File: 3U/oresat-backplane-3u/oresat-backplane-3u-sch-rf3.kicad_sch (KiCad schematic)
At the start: 30 parts

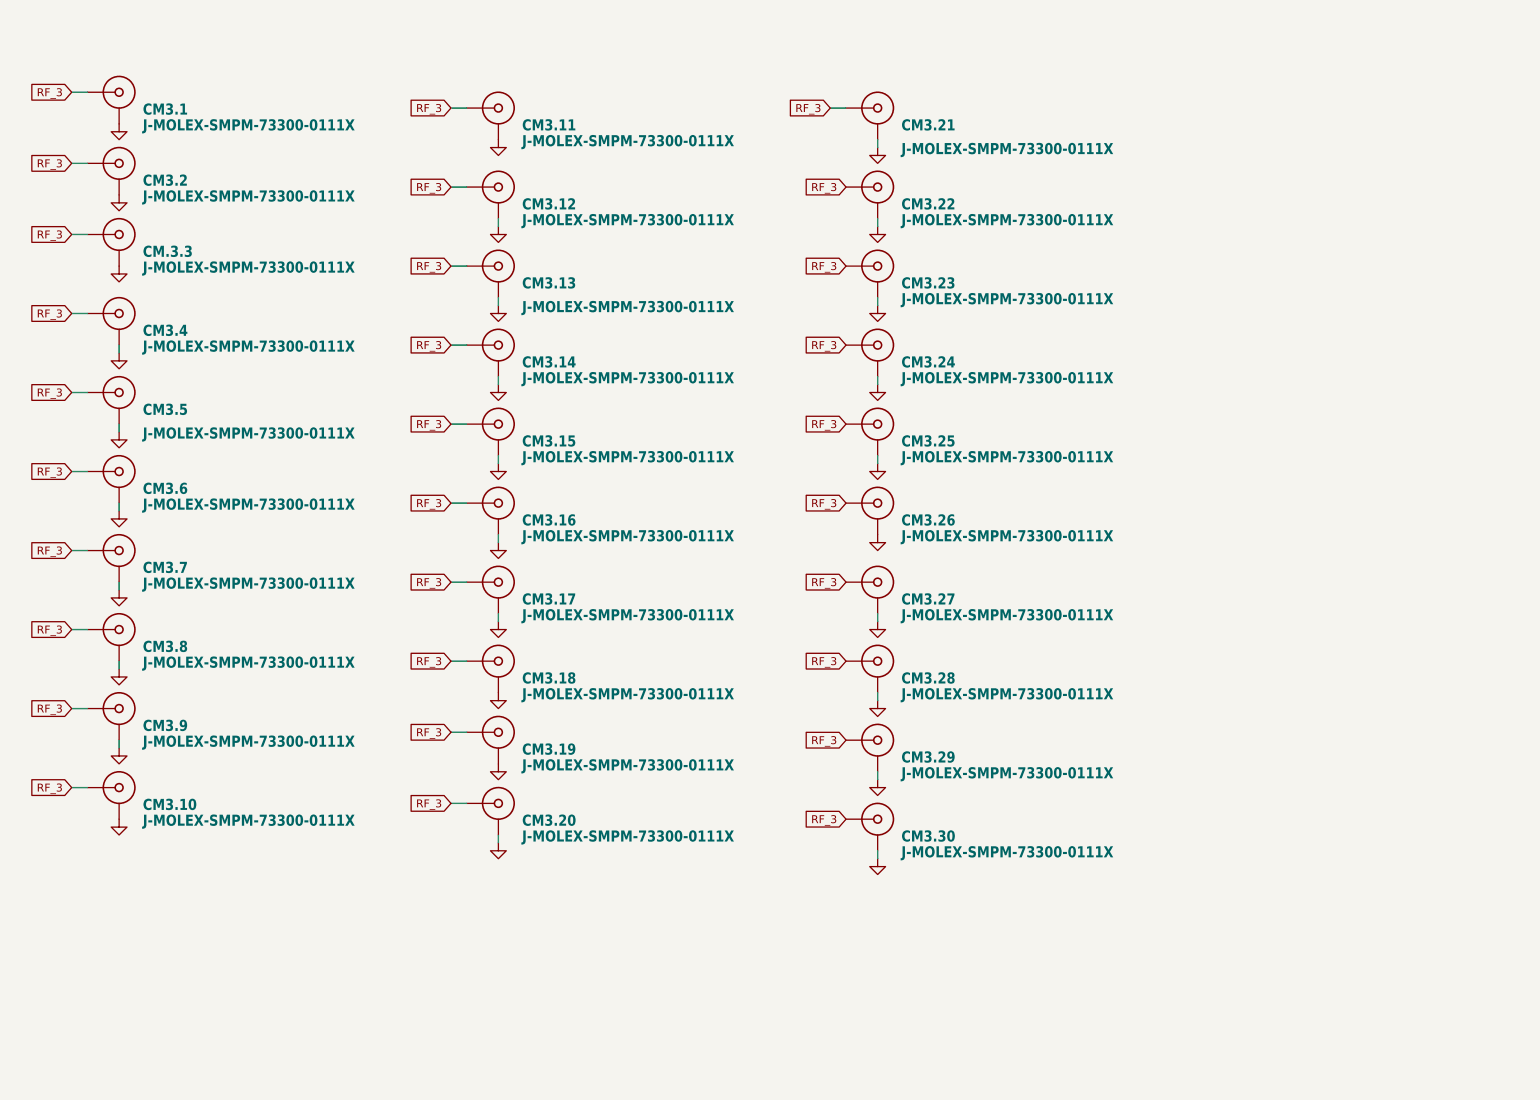
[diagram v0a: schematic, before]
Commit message: Moved can lines to back & fixed RF schematic organization
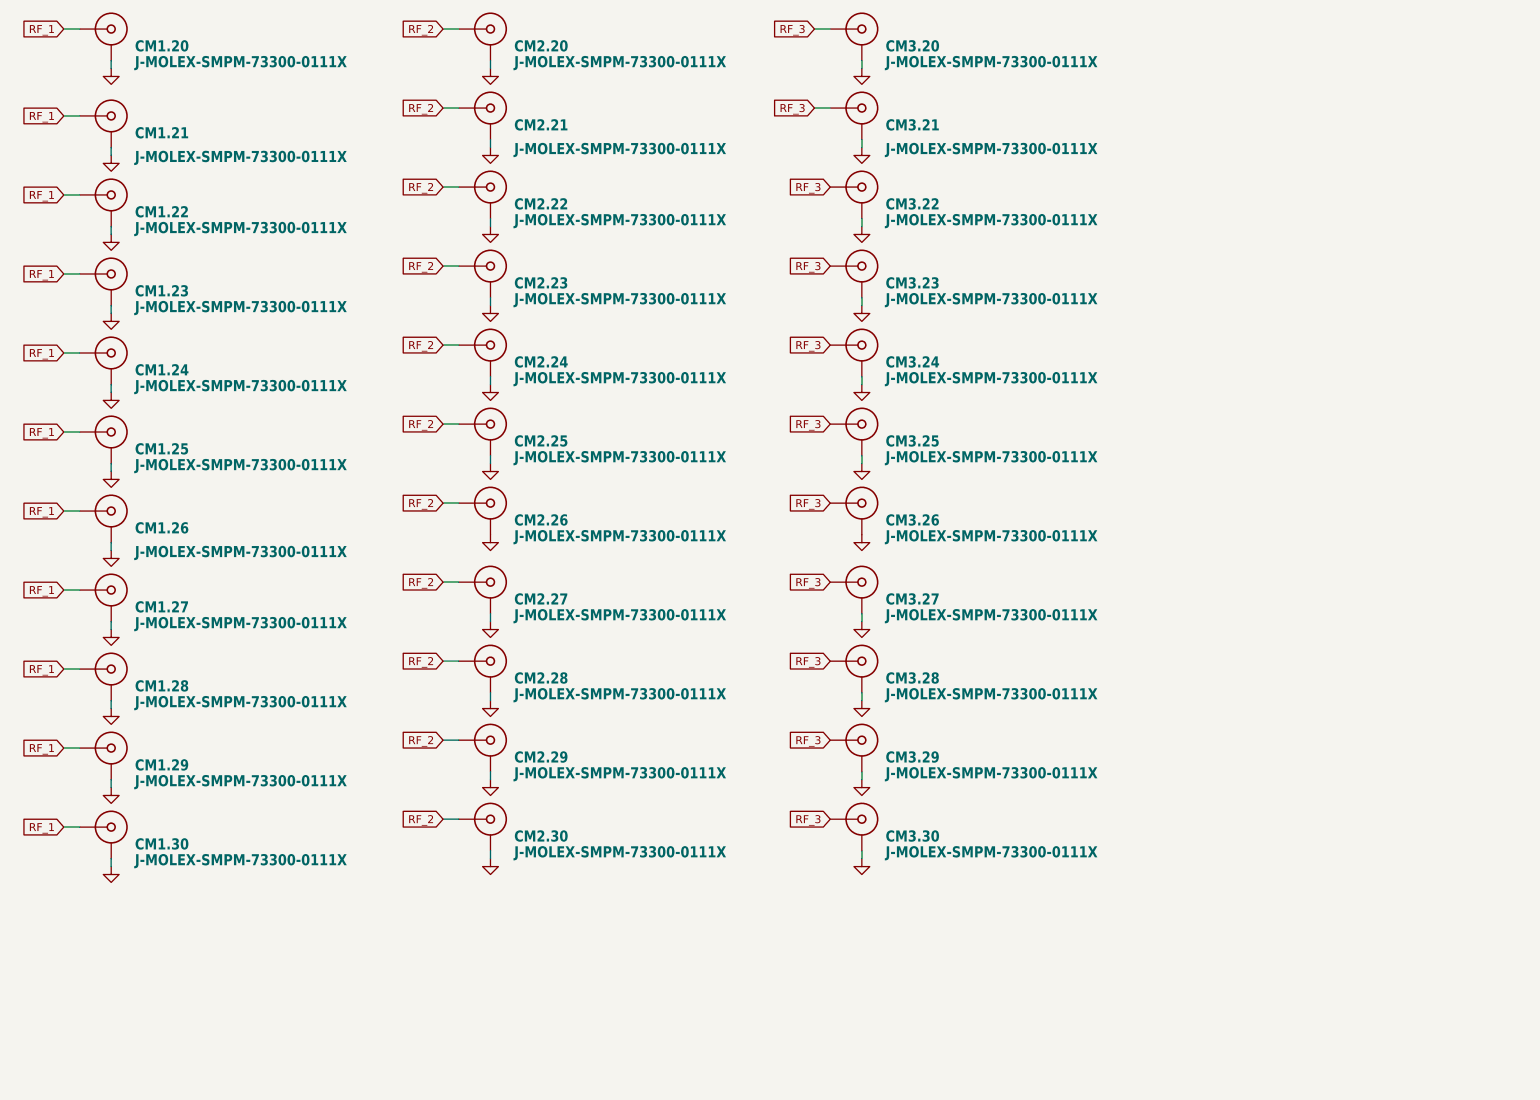
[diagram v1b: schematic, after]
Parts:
- removed CM.3.3, CM3.1, CM3.10, CM3.11, CM3.12, CM3.13, CM3.14, CM3.15, CM3.16, CM3.17, CM3.18, CM3.19, CM3.2, CM3.4, CM3.5, CM3.6, CM3.7, CM3.8, CM3.9: J-MOLEX-SMPM-73300-0111X, oresat-connectors:J-MOLEX-SMPM-73300-0111X-long, symbol oresat-connectors:J-MOLEX-SMPM-73300-0111X_1
- added CM1.20, CM1.21, CM1.22, CM1.23, CM1.24, CM1.25, CM1.26, CM1.27, CM1.28, CM1.29, CM1.30, CM2.20, CM2.21, CM2.22, CM2.23, CM2.24, CM2.25, CM2.26, CM2.27, CM2.28, CM2.29, CM2.30: J-MOLEX-SMPM-73300-0111X, oresat-connectors:J-MOLEX-SMPM-73300-0111X-long, symbol oresat-connectors:J-MOLEX-SMPM-73300-0111X_1
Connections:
- net GND: now also CM1.20.GND (SHIELD1), CM1.21.GND (SHIELD1), CM1.22.GND (SHIELD1), CM1.23.GND (SHIELD1), CM1.24.GND (SHIELD1), CM1.25.GND (SHIELD1), CM1.26.GND (SHIELD1), CM1.27.GND (SHIELD1), CM1.28.GND (SHIELD1), CM1.29.GND (SHIELD1), CM1.30.GND (SHIELD1), CM2.20.GND (SHIELD1), CM2.21.GND (SHIELD1), CM2.22.GND (SHIELD1), CM2.23.GND (SHIELD1), CM2.24.GND (SHIELD1), CM2.25.GND (SHIELD1), CM2.26.GND (SHIELD1), CM2.27.GND (SHIELD1), CM2.28.GND (SHIELD1), CM2.29.GND (SHIELD1), CM2.30.GND (SHIELD1)
- new net RF_1: CM1.20.RF-DOWN (RF), CM1.21.RF-DOWN (RF), CM1.22.RF-DOWN (RF), CM1.23.RF-DOWN (RF), CM1.24.RF-DOWN (RF), CM1.25.RF-DOWN (RF), CM1.26.RF-DOWN (RF), CM1.27.RF-DOWN (RF), CM1.28.RF-DOWN (RF), CM1.29.RF-DOWN (RF), CM1.30.RF-DOWN (RF)
- new net RF_2: CM2.20.RF-DOWN (RF), CM2.21.RF-DOWN (RF), CM2.22.RF-DOWN (RF), CM2.23.RF-DOWN (RF), CM2.24.RF-DOWN (RF), CM2.25.RF-DOWN (RF), CM2.26.RF-DOWN (RF), CM2.27.RF-DOWN (RF), CM2.28.RF-DOWN (RF), CM2.29.RF-DOWN (RF), CM2.30.RF-DOWN (RF)
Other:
- moved on the sheet: CM3.20, CM3.21, CM3.22, CM3.23, CM3.24, CM3.25, CM3.26, CM3.27, CM3.28, CM3.29, CM3.30

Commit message: Updated generic 3U backplane with correct fastener copper and solder mask cutouts under fastners, and updated date on sch and brd.
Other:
- company: (none) -> Portland State Aerospace Society
- title: (none) -> Generic OreSat 3U Backplane
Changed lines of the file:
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@@
 	(generator "eeschema")
 	(generator_version "9.0")
-	(paper "A4")
+	(paper "B")
+	(title_block
+		(title "Generic OreSat 3U Backplane")
+		(date "2026-02-20")
+		(rev "1.0")
+		(company "Portland State Aerospace Society")
+	)
 	(wire
 		(pts

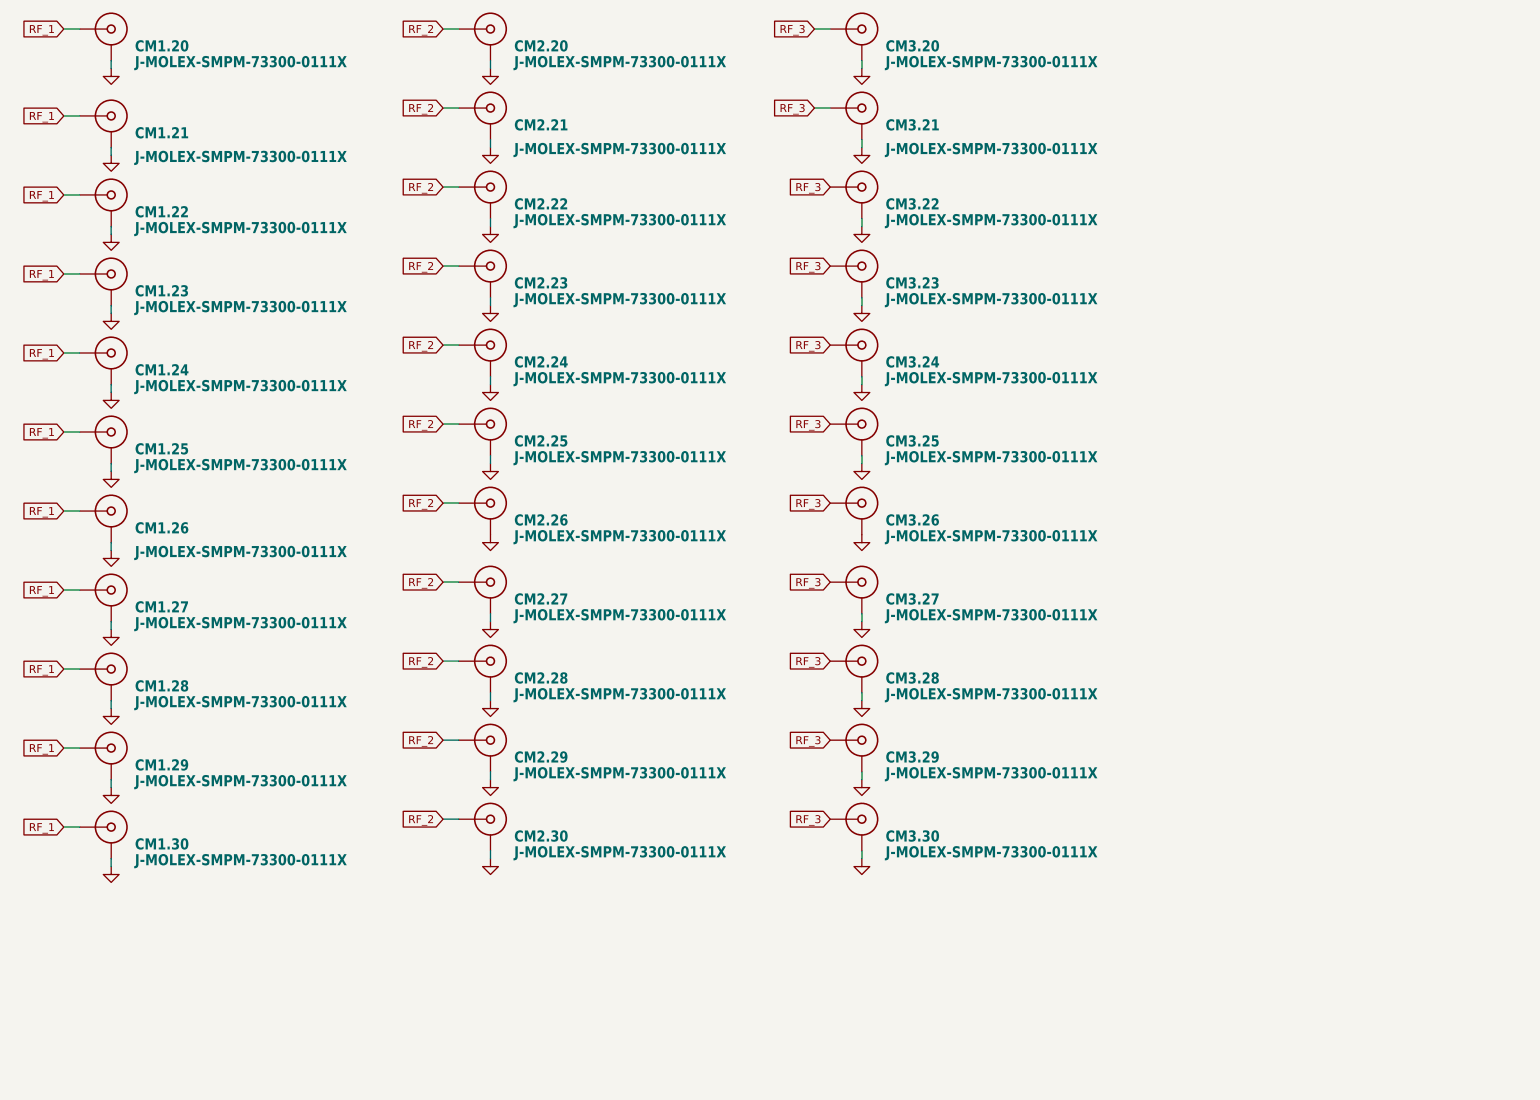
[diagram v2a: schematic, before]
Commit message: Connected Spares and switched OPD to inner layer. Updated RF cons -- **RF con new footprint has ground pad schematic parity error
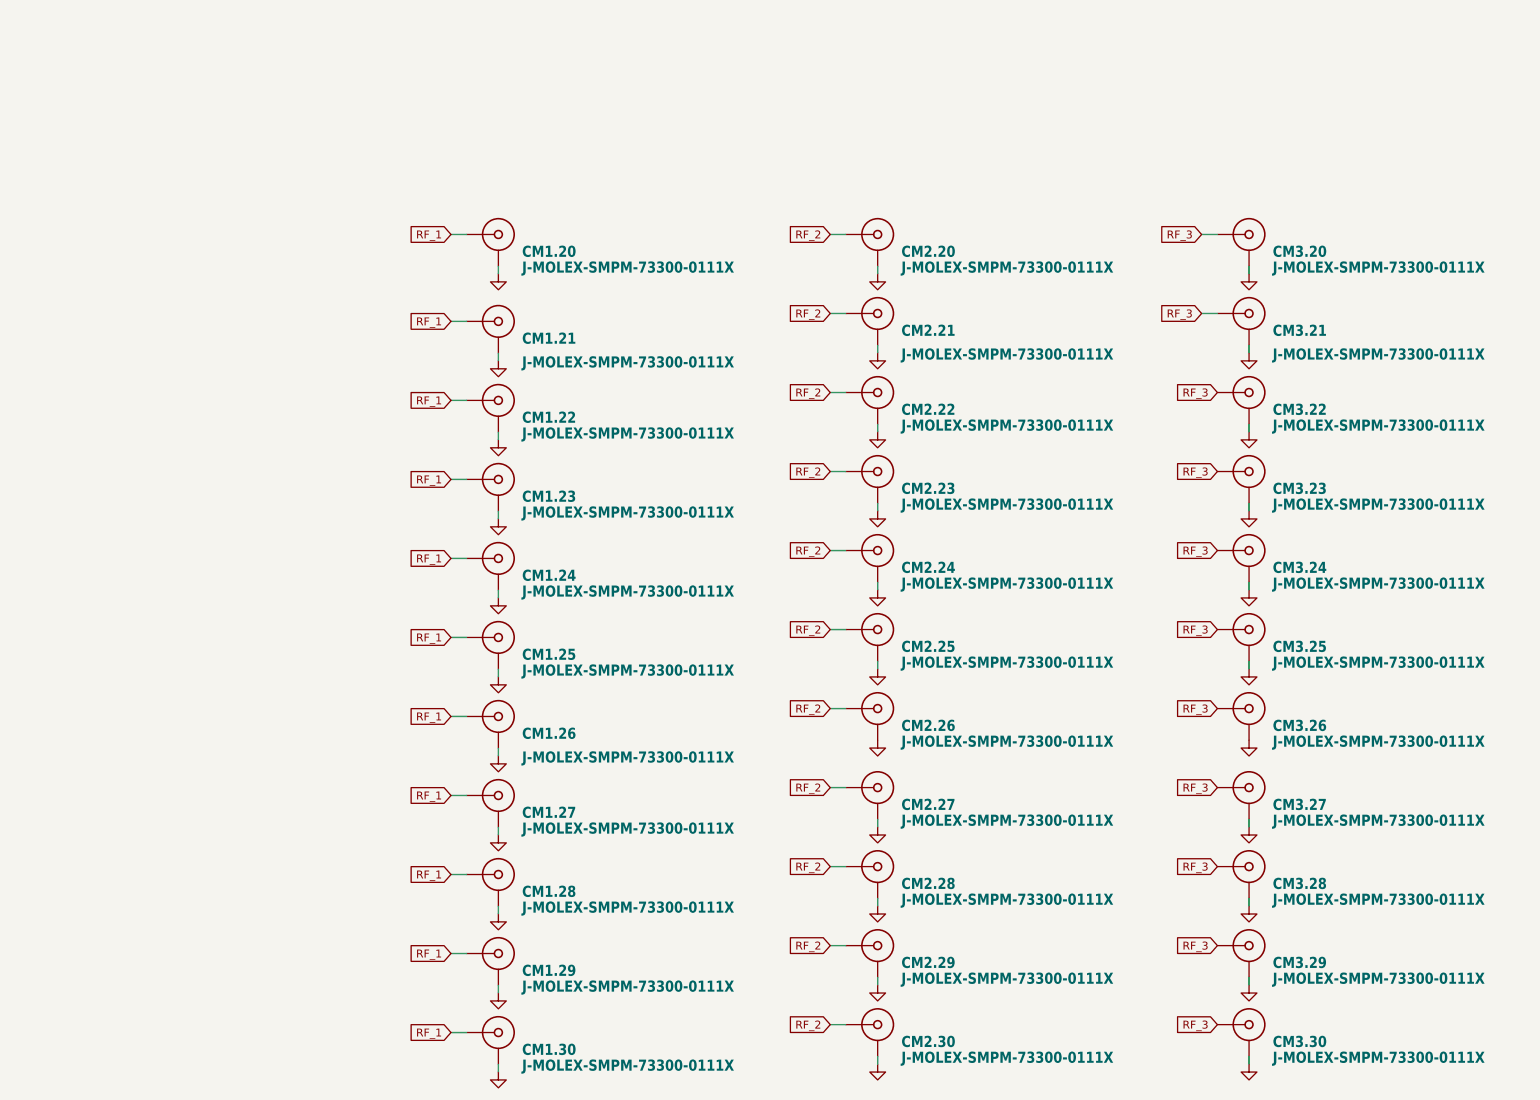
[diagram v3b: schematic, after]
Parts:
- CM1.20, CM1.21, CM1.22, CM1.23, CM1.24, CM1.25, CM1.26, CM1.27, CM1.28, CM1.29, CM1.30, CM2.20, CM2.21, CM2.22, CM2.23, CM2.24, CM2.25, CM2.26, CM2.27, CM2.28, CM2.29, CM2.30, CM3.20, CM3.21, CM3.22, CM3.23, CM3.24, CM3.25, CM3.26, CM3.27, CM3.28, CM3.29, CM3.30: footprint oresat-connectors:J-MOLEX-SMPM-73300-0111X-long -> oresat-connectors:J-MOLEX-SMPM-73300-011X
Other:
- moved on the sheet: CM1.20, CM1.21, CM1.22, CM1.23, CM1.24, CM1.25, CM1.26, CM1.27, CM1.28, CM1.29, CM1.30, CM2.20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

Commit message: Updated schematic symbol for RF con. Believe this is done. Remaining DRC errors are only unconnected RF cons -- fine until use defined for non-generic version.
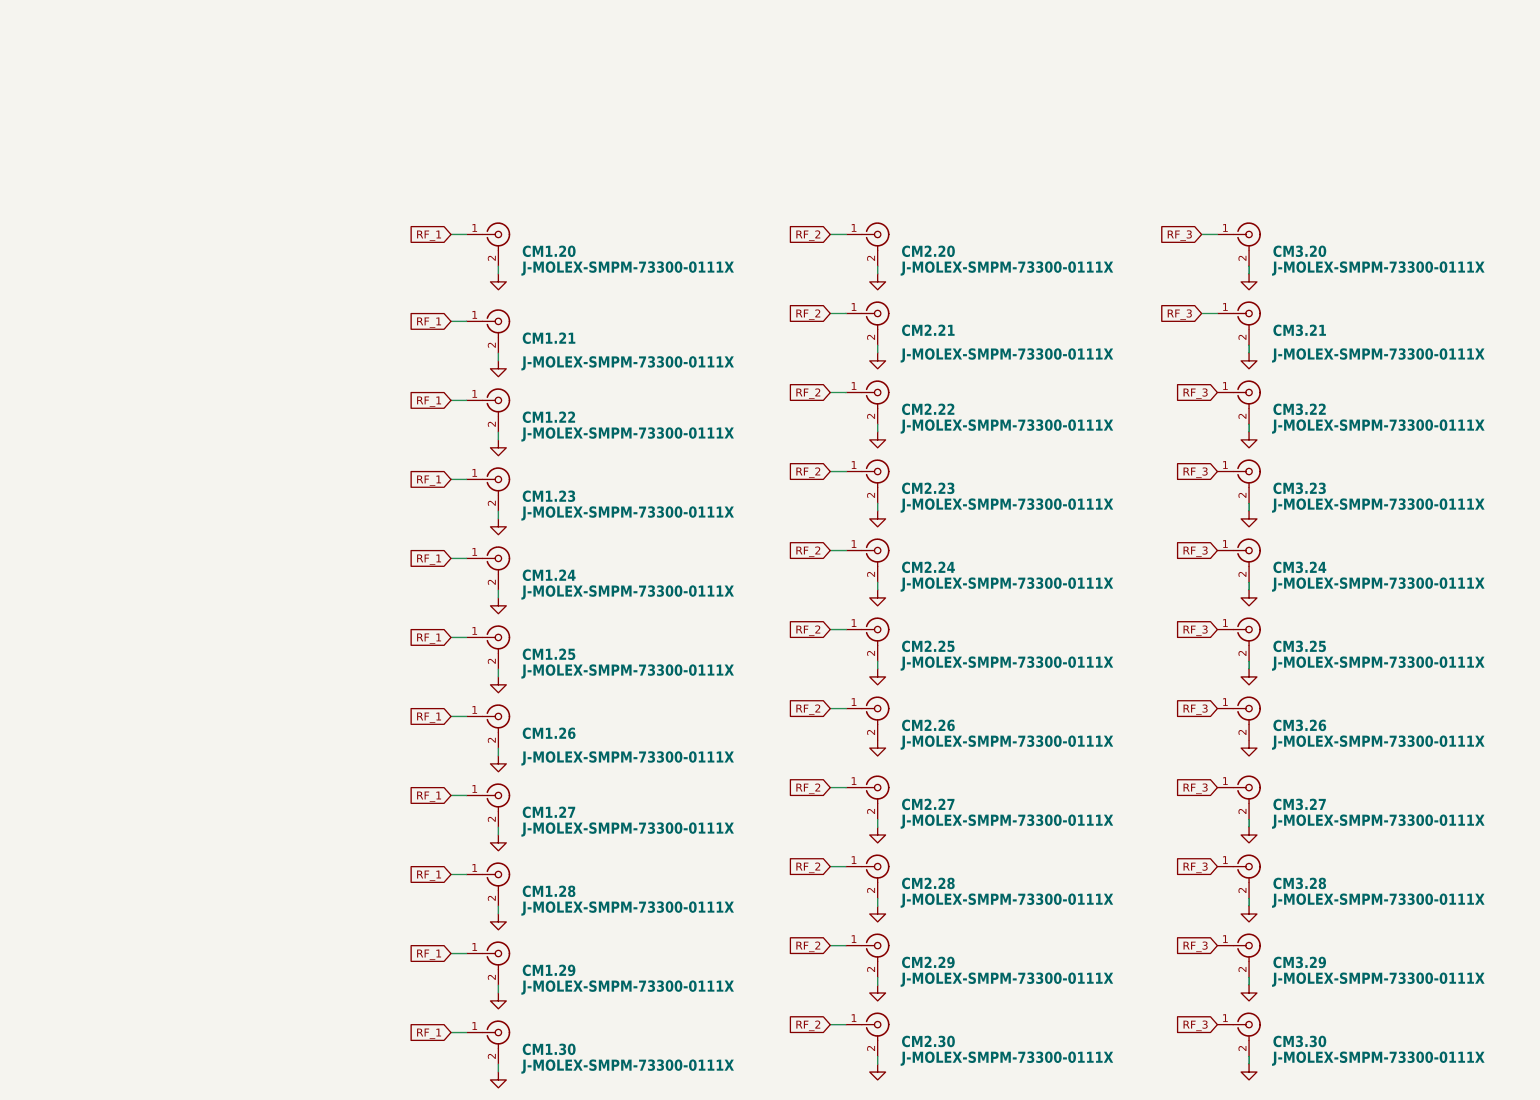
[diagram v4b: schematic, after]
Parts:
- CM1.20, CM1.21, CM1.22, CM1.23, CM1.24, CM1.25, CM1.26, CM1.27, CM1.28, CM1.29, CM1.30, CM2.20, CM2.21, CM2.22, CM2.23, CM2.24, CM2.25, CM2.26, CM2.27, CM2.28, CM2.29, CM2.30, CM3.20, CM3.21, CM3.22, CM3.23, CM3.24, CM3.25, CM3.26, CM3.27, CM3.28, CM3.29, CM3.30: symbol oresat-connectors:J-MOLEX-SMPM-73300-0111X_1 -> Connector:Conn_Coaxial
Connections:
- net GND: now also CM1.20.2 (Ext), CM1.21.2 (Ext), CM1.22.2 (Ext), CM1.23.2 (Ext), CM1.24.2 (Ext), CM1.25.2 (Ext), CM1.26.2 (Ext), CM1.27.2 (Ext), CM1.28.2 (Ext), CM1.29.2 (Ext), CM1.30.2 (Ext), CM2.20.2 (Ext), CM2.21.2 (Ext), CM2.22.2 (Ext), CM2.23.2 (Ext), CM2.24.2 (Ext), CM2.25.2 (Ext), CM2.26.2 (Ext), CM2.27.2 (Ext), CM2.28.2 (Ext), CM2.29.2 (Ext), CM2.30.2 (Ext), CM3.20.2 (Ext), CM3.21.2 (Ext), CM3.22.2 (Ext), CM3.23.2 (Ext), CM3.24.2 (Ext), CM3.25.2 (Ext), CM3.26.2 (Ext), CM3.27.2 (Ext), CM3.28.2 (Ext), CM3.29.2 (Ext), CM3.30.2 (Ext); no longer CM1.20.GND (SHIELD1), CM1.21.GND (SHIELD1), CM1.22.GND (SHIELD1), CM1.23.GND (SHIELD1), CM1.24.GND (SHIELD1), CM1.25.GND (SHIELD1), CM1.26.GND (SHIELD1), CM1.27.GND (SHIELD1), CM1.28.GND (SHIELD1), CM1.29.GND (SHIELD1), CM1.30.GND (SHIELD1), CM2.20.GND (SHIELD1), CM2.21.GND (SHIELD1), CM2.22.GND (SHIELD1), CM2.23.GND (SHIELD1), CM2.24.GND (SHIELD1), CM2.25.GND (SHIELD1), CM2.26.GND (SHIELD1), CM2.27.GND (SHIELD1), CM2.28.GND (SHIELD1), CM2.29.GND (SHIELD1), CM2.30.GND (SHIELD1), CM3.20.GND (SHIELD1), CM3.21.GND (SHIELD1), CM3.22.GND (SHIELD1), CM3.23.GND (SHIELD1), CM3.24.GND (SHIELD1), CM3.25.GND (SHIELD1), CM3.26.GND (SHIELD1), CM3.27.GND (SHIELD1), CM3.28.GND (SHIELD1), CM3.29.GND (SHIELD1), CM3.30.GND (SHIELD1)
- net RF_1: now also CM1.20.1 (In), CM1.21.1 (In), CM1.22.1 (In), CM1.23.1 (In), CM1.24.1 (In), CM1.25.1 (In), CM1.26.1 (In), CM1.27.1 (In), CM1.28.1 (In), CM1.29.1 (In), CM1.30.1 (In); no longer CM1.20.RF-DOWN (RF), CM1.21.RF-DOWN (RF), CM1.22.RF-DOWN (RF), CM1.23.RF-DOWN (RF), CM1.24.RF-DOWN (RF), CM1.25.RF-DOWN (RF), CM1.26.RF-DOWN (RF), CM1.27.RF-DOWN (RF), CM1.28.RF-DOWN (RF), CM1.29.RF-DOWN (RF), CM1.30.RF-DOWN (RF)
- net RF_2: now also CM2.20.1 (In), CM2.21.1 (In), CM2.22.1 (In), CM2.23.1 (In), CM2.24.1 (In), CM2.25.1 (In), CM2.26.1 (In), CM2.27.1 (In), CM2.28.1 (In), CM2.29.1 (In), CM2.30.1 (In); no longer CM2.20.RF-DOWN (RF), CM2.21.RF-DOWN (RF), CM2.22.RF-DOWN (RF), CM2.23.RF-DOWN (RF), CM2.24.RF-DOWN (RF), CM2.25.RF-DOWN (RF), CM2.26.RF-DOWN (RF), CM2.27.RF-DOWN (RF), CM2.28.RF-DOWN (RF), CM2.29.RF-DOWN (RF), CM2.30.RF-DOWN (RF)
- net RF_3: now also CM3.20.1 (In), CM3.21.1 (In), CM3.22.1 (In), CM3.23.1 (In), CM3.24.1 (In), CM3.25.1 (In), CM3.26.1 (In), CM3.27.1 (In), CM3.28.1 (In), CM3.29.1 (In), CM3.30.1 (In); no longer CM3.20.RF-DOWN (RF), CM3.21.RF-DOWN (RF), CM3.22.RF-DOWN (RF), CM3.23.RF-DOWN (RF), CM3.24.RF-DOWN (RF), CM3.25.RF-DOWN (RF), CM3.26.RF-DOWN (RF), CM3.27.RF-DOWN (RF), CM3.28.RF-DOWN (RF), CM3.29.RF-DOWN (RF), CM3.30.RF-DOWN (RF)
